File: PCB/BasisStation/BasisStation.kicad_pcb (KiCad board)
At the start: 2 copper layers, 160 x 135 mm, 20 parts, among them J1 Conn_02x05_Odd_Even, U2 ESP32-S3-WROOM-2

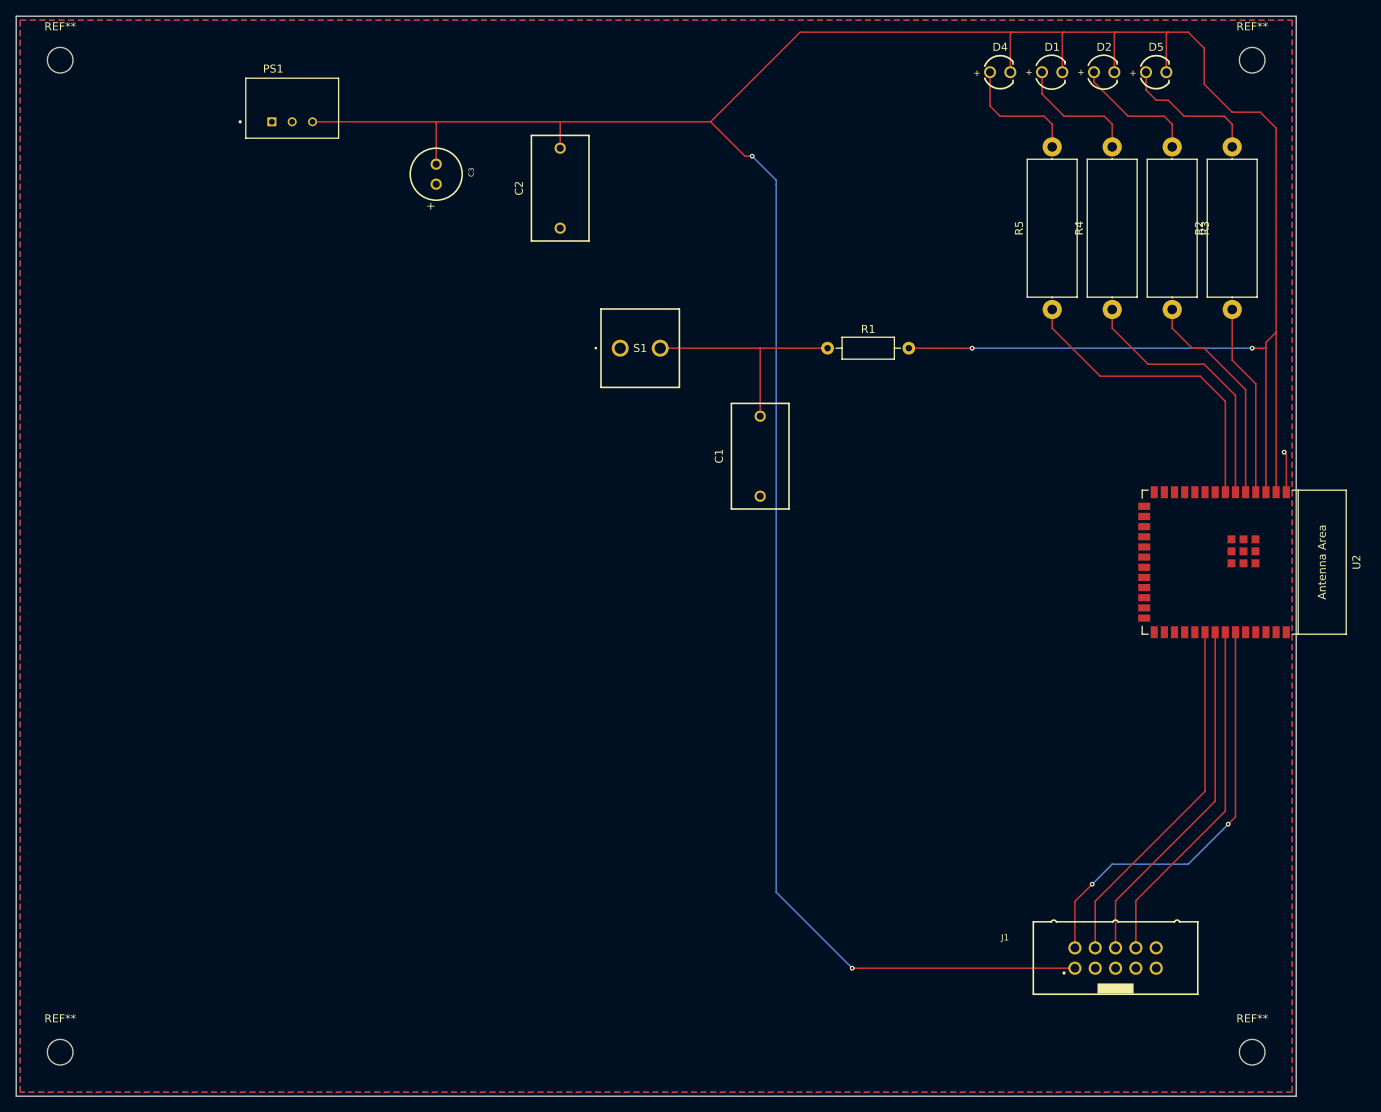
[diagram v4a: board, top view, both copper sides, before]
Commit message: 6Pin header male hinzugefügt und Leiterbahnen optimiert
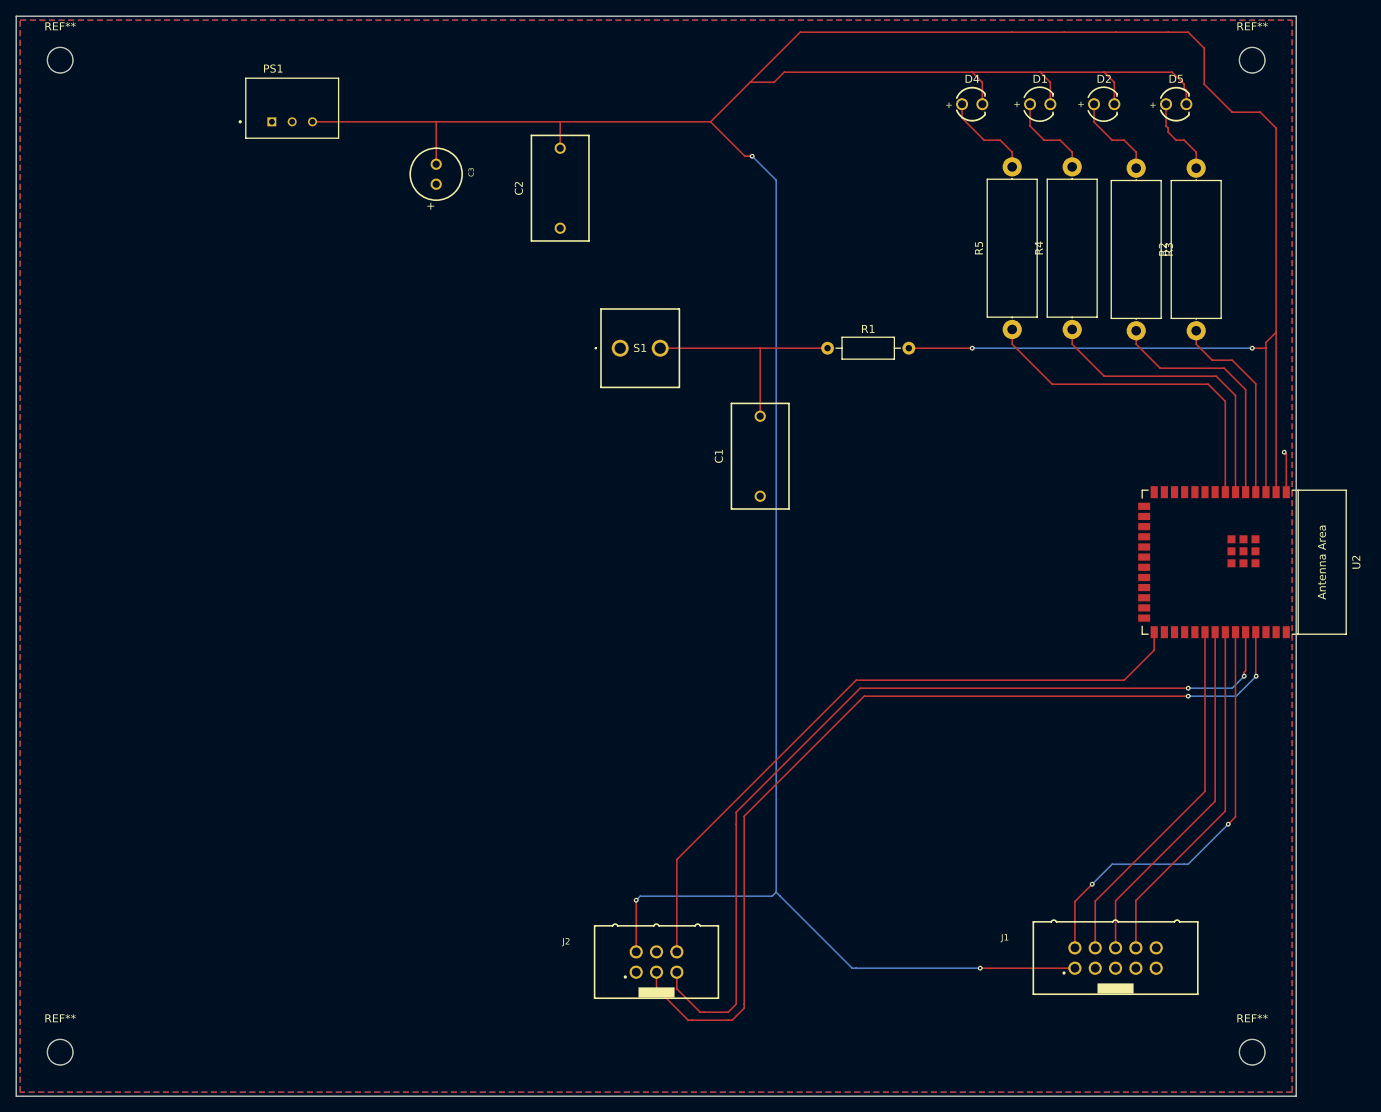
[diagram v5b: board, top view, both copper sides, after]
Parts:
- added J2: Conn_02x03_Odd_Even, Footprints:61200621621, F.Cu at (130.0, 143.2)
- moved R4 5.59 mm to (182.0, 64.2)
- moved R5 5.59 mm to (174.5, 64.2)
- moved D4 5.32 mm to (169.5, 36.0)
- moved R2 5.23 mm to (197.5, 64.3)
- moved R3 5.23 mm to (190.0, 44.0)
- moved D5 4.72 mm to (195.0, 36.0)
- moved D1 4.27 mm to (178.0, 36.0)
- moved D2 4.00 mm to (186.0, 36.0)
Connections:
- net MTCK renamed Net-(J1-Pin_4)
- net MTDI renamed Net-(J1-Pin_8)
- net MTDO renamed Net-(J1-Pin_6)
- net MTMS renamed Net-(J1-Pin_2)
- D4 pad 1: +3V3 -> Net-(D4-A)
- D4 pad 2: Net-(D4-A) -> +3V3
- U2 pad 27: unconnected-(U2-GPIO0/BOOT-Pad27) -> IO0
- U2 pad 3: EN -> /EN
- U2 pad 36: unconnected-(U2-U0RXD/GPIO44/CLK_OUT2-Pad36) -> RXD0
- U2 pad 37: unconnected-(U2-U0TXD/GPIO43/CLK_OUT1-Pad37) -> TXD0
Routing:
- net TXD0: track 0.00 -> 116.0 mm, vias 0 -> 2
- net RXD0: track 0.00 -> 111.2 mm, vias 0 -> 2
- net IO0: track 0.00 -> 84.3 mm
- net +3V3: track 413.8 -> 489.4 mm, vias 4 -> 5
- net Net-(D5-Pad1): track 17.6 -> 10.1 mm
- net Net-(D2-A): track 16.0 -> 11.1 mm
- net Net-(D1-A): track 15.9 -> 11.2 mm
- net Net-(D4-A): track 15.8 -> 11.6 mm
- net Net-(U2-GPIO7/TOUCH7/ADC1_CH6): track 39.1 -> 42.8 mm
- net Net-(U2-GPIO6/TOUCH6/ADC1_CH5): track 33.3 -> 37.0 mm
- net Net-(U2-GPIO5/TOUCH5/ADC1_CH4): track 27.5 -> 30.5 mm
- net Net-(U2-GPIO4/TOUCH4/ADC1_CH3): track 24.1 -> 24.7 mm

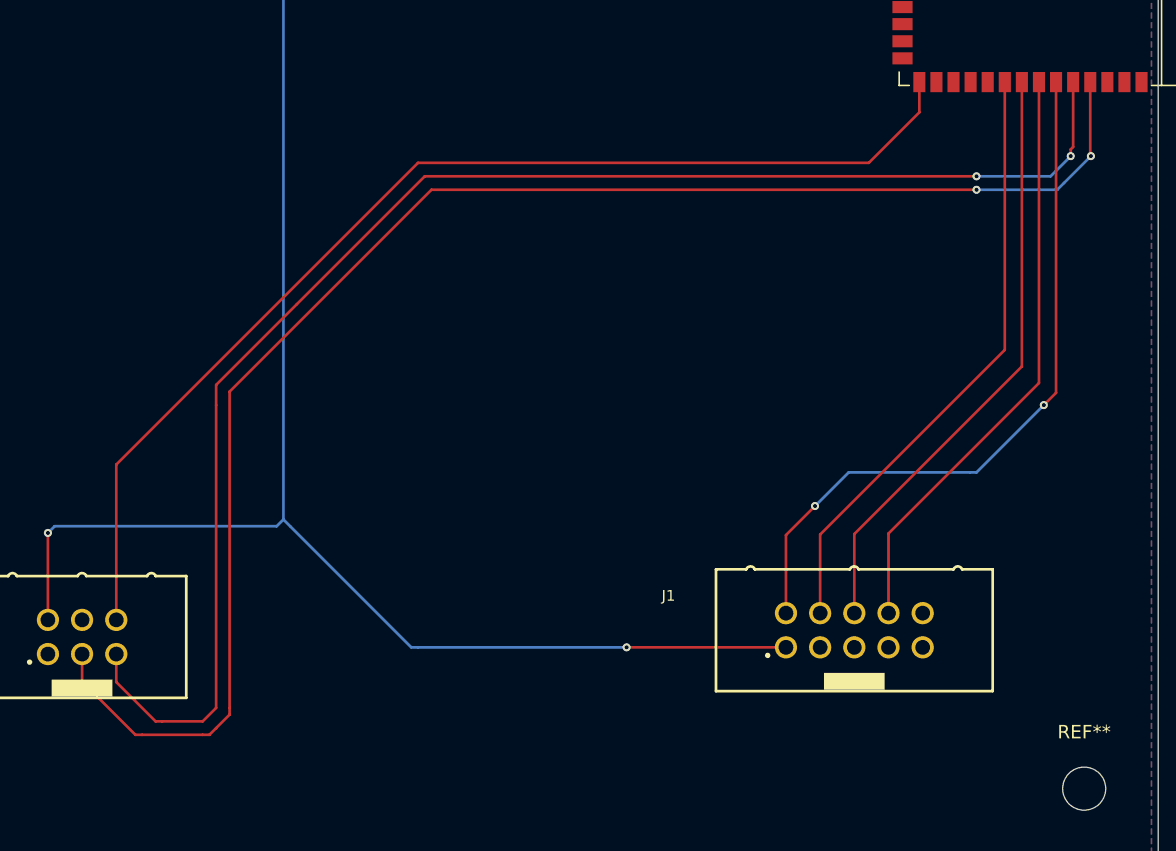
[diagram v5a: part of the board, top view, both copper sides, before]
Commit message: Leiterbahnen überarbeitet
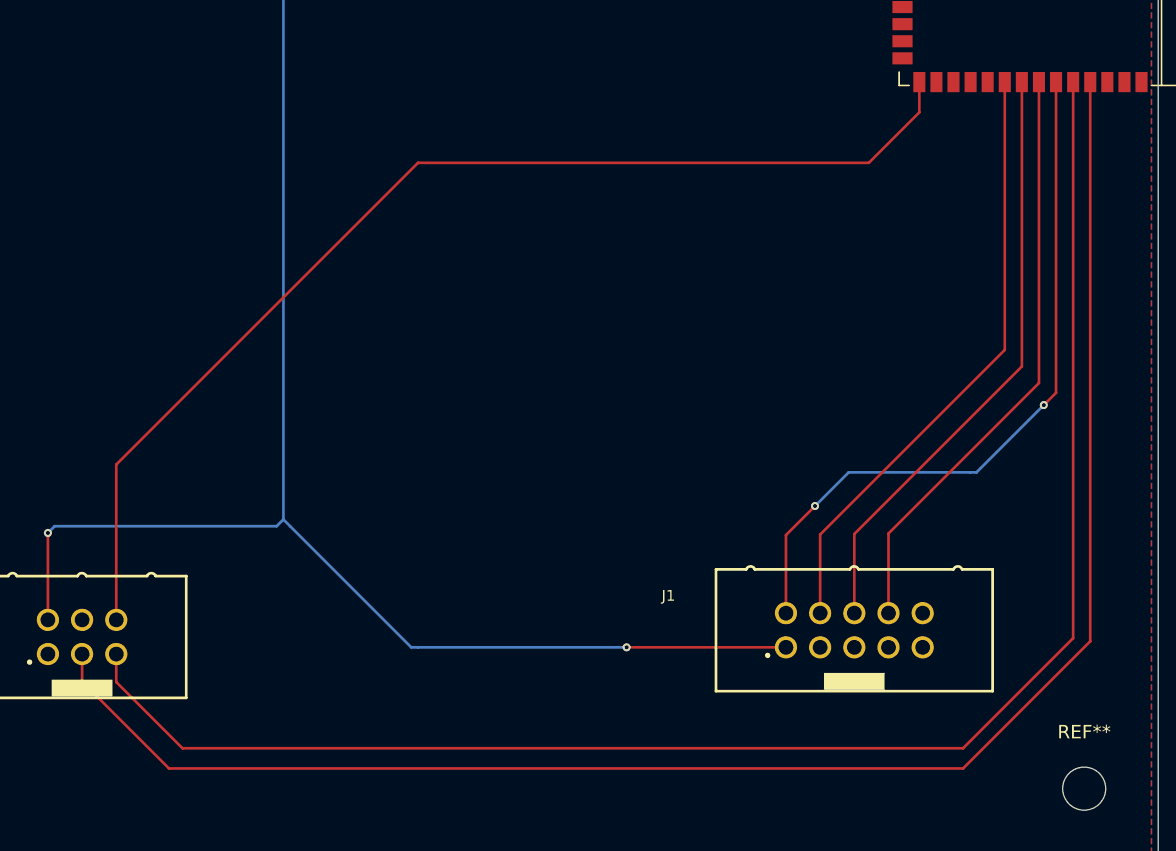
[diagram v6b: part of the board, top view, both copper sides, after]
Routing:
- net TXD0: track 116.0 -> 125.1 mm, vias 2 -> 0
- net RXD0: track 111.2 -> 119.9 mm, vias 2 -> 0
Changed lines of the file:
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@@
 	)
 	(segment
-		(start 132.58 146.58)
-		(end 135.5 149.5)
-		(width 0.2)
-		(layer "F.Cu")
-		(net 46)
-	)
-	(segment
-		(start 203.5 107.5)
-		(end 203.5 107)
-		(width 0.2)
-		(layer "F.Cu")
-		(net 46)
-	)
-	(segment
-		(start 140 126)
-		(end 140 124.5)
-		(width 0.2)
-		(layer "F.Cu")
-		(net 46)
-	)
-	(segment
-		(start 135.5 149.5)
-		(end 136 149.5)
-		(width 0.2)
-		(layer "F.Cu")
-		(net 46)
-	)
-	(segment
-		(start 146 118.5)
-		(end 155.5 109)
-		(width 0.2)
-		(layer "F.Cu")
-		(net 46)
-	)
-	(segment
-		(start 132.58 144.5)
+		(start 137.5 151.5)
 		(end 132.58 146.58)
 		(width 0.2)
@@
 	)
 	(segment
-		(start 140 124.5)
-		(end 146 118.5)
+		(start 203.68 143.32)
+		(end 195.5 151.5)
 		(width 0.2)
 		(layer "F.Cu")
@@
 	)
 	(segment
-		(start 136 149.5)
-		(end 139 149.5)
+		(start 203.68 102)
+		(end 203.68 143.32)
 		(width 0.2)
 		(layer "F.Cu")
@@
 	)
 	(segment
-		(start 155.5 109)
-		(end 196.5 109)
+		(start 132.58 146.58)
+		(end 132.58 144.5)
 		(width 0.2)
 		(layer "F.Cu")
@@
 	)
 	(segment
-		(start 140 148.5)
-		(end 140 126)
+		(start 195.5 151.5)
+		(end 137.5 151.5)
 		(width 0.2)
 		(layer "F.Cu")
@@
 	)
 	(segment
-		(start 139 149.5)
-		(end 140 148.5)
-		(width 0.2)
-		(layer "F.Cu")
-		(net 46)
-	)
-	(segment
-		(start 203.5 107)
-		(end 203.68 106.82)
-		(width 0.2)
-		(layer "F.Cu")
-		(net 46)
-	)
-	(segment
-		(start 203.68 106.82)
-		(end 203.68 102)
-		(width 0.2)
-		(layer "F.Cu")
-		(net 46)
-	)
-	(via
-		(at 203.5 107.5)
-		(size 0.6)
-		(drill 0.3)
-		(layers "F.Cu" "B.Cu")
-		(net 46)
-	)
-	(via
-		(at 196.5 109)
-		(size 0.6)
-		(drill 0.3)
-		(layers "F.Cu" "B.Cu")
-		(net 46)
-	)
-	(segment
-		(start 202 109)
-		(end 203.5 107.5)
-		(width 0.2)
-		(layer "B.Cu")
-		(net 46)
-	)
-	(segment
-		(start 196.5 109)
-		(end 202 109)
-		(width 0.2)
-		(layer "B.Cu")
-		(net 46)
-	)
-	(segment
-		(start 141 148.5)
-		(end 141 125)
+		(start 204.95 143.55)
+		(end 195.5 153)
 		(width 0.2)
 		(layer "F.Cu")
@@
 	)
 	(segment
-		(start 156 110)
-		(end 196.5 110)
+		(start 136.5 153)
+		(end 130.04 146.54)
+		(width 0.2)
+		(layer "F.Cu")
+		(net 47)
+	)
+	(segment
+		(start 195.5 153)
+		(end 136.5 153)
+		(width 0.2)
+		(layer "F.Cu")
+		(net 47)
+	)
+	(segment
+		(start 204.95 102)
+		(end 204.95 143.55)
 		(width 0.2)
 		(layer "F.Cu")
@@
 	(segment
 		(start 130.04 146.54)
-		(end 134 150.5)
+		(end 130.04 144.5)
 		(width 0.2)
 		(layer "F.Cu")
 		(net 47)
 	)
-	(segment
-		(start 134.5 150.5)
-		(end 139 150.5)
-		(width 0.2)
-		(layer "F.Cu")
-		(net 47)
-	)
-	(segment
-		(start 205 107.5)
-		(end 204.95 107.45)
-		(width 0.2)
-		(layer "F.Cu")
-		(net 47)
-	)
-	(segment
-		(start 139.5 150.5)
-		(end 140 150)
-		(width 0.2)
-		(layer "F.Cu")
-		(net 47)
-	)
-	(segment
-		(start 141 125)
-		(end 156 110)
-		(width 0.2)
-		(layer "F.Cu")
-		(net 47)
-	)
-	(segment
-		(start 204.95 107.45)
-		(end 204.95 102)
-		(width 0.2)
-		(layer "F.Cu")
-		(net 47)
-	)
-	(segment
-		(start 130.04 144.5)
-		(end 130.04 146.54)
-		(width 0.2)
-		(layer "F.Cu")
-		(net 47)
-	)
-	(segment
-		(start 140 150)
-		(end 141 149)
-		(width 0.2)
-		(layer "F.Cu")
-		(net 47)
-	)
-	(segment
-		(start 141 149)
-		(end 141 148.5)
-		(width 0.2)
-		(layer "F.Cu")
-		(net 47)
-	)
-	(segment
-		(start 139 150.5)
-		(end 139.5 150.5)
-		(width 0.2)
-		(layer "F.Cu")
-		(net 47)
-	)
-	(segment
-		(start 134 150.5)
-		(end 134.5 150.5)
-		(width 0.2)
-		(layer "F.Cu")
-		(net 47)
-	)
-	(via
-		(at 196.5 110)
-		(size 0.6)
-		(drill 0.3)
-		(layers "F.Cu" "B.Cu")
-		(net 47)
-	)
-	(via
-		(at 205 107.5)
-		(size 0.6)
-		(drill 0.3)
-		(layers "F.Cu" "B.Cu")
-		(net 47)
-	)
-	(segment
-		(start 196.5 110)
-		(end 202.5 110)
-		(width 0.2)
-		(layer "B.Cu")
-		(net 47)
-	)
-	(segment
-		(start 203 109.5)
-		(end 205 107.5)
-		(width 0.2)
-		(layer "B.Cu")
-		(net 47)
-	)
-	(segment
-		(start 202.5 110)
-		(end 203 109.5)
-		(width 0.2)
-		(layer "B.Cu")
-		(net 47)
-	)
